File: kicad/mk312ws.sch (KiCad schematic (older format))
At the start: 14 parts, among them J1 Conn_01x06_Male, Q1 BSS138, Q2 BSS138, Q3 BSS138, Q4 BSS138, U1 mini_esp32

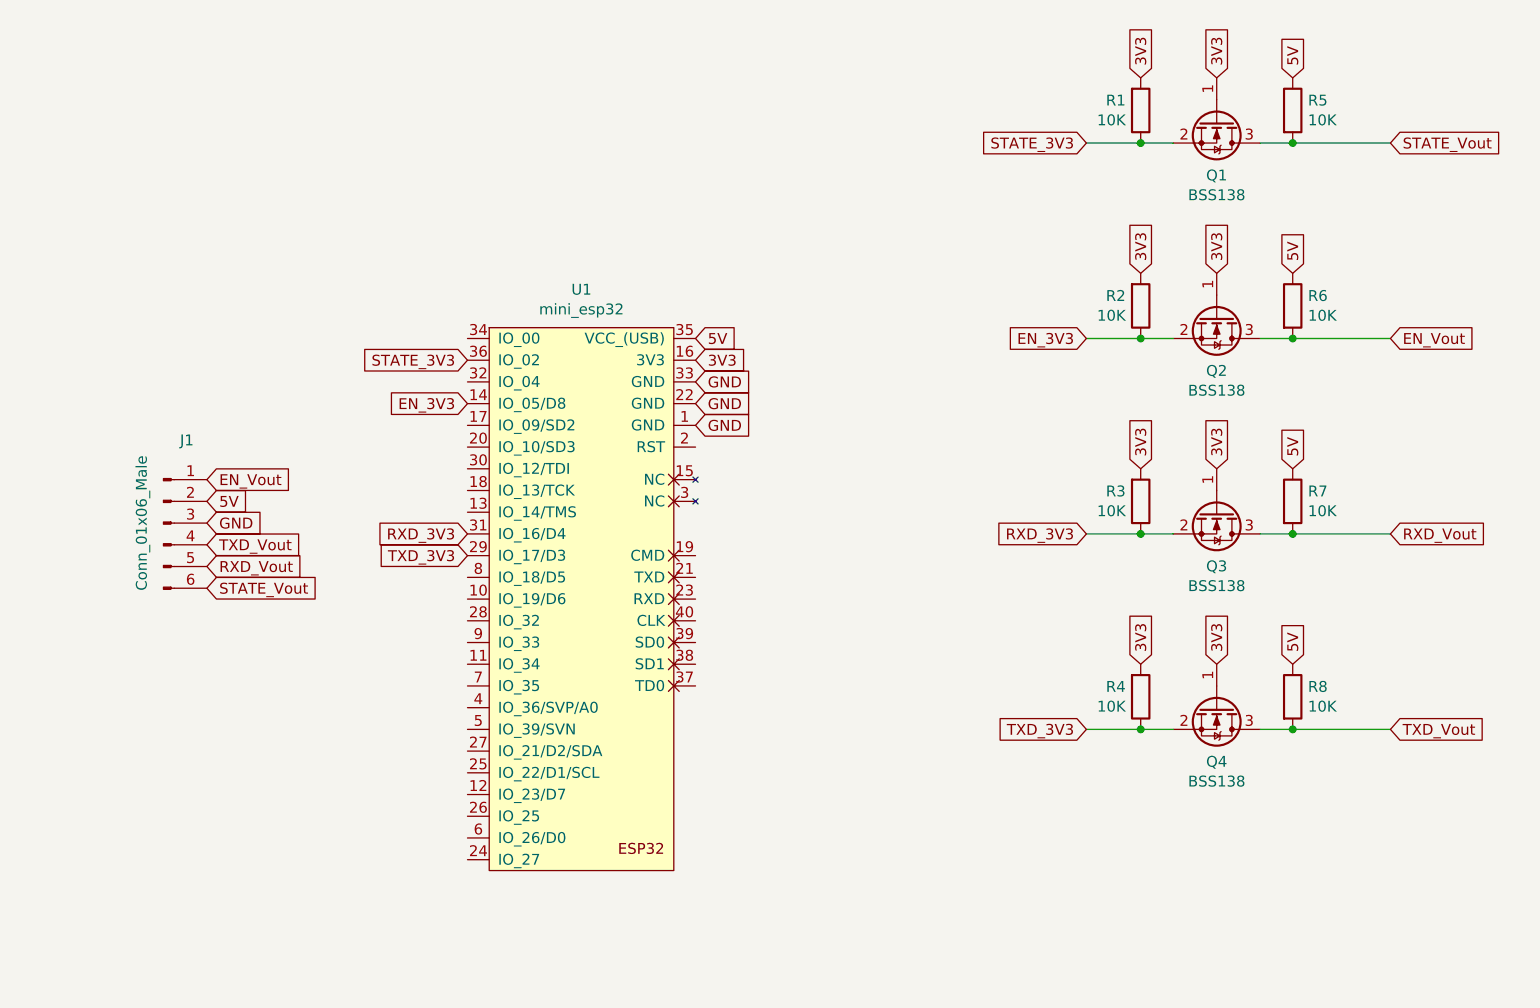
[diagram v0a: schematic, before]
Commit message: adapter v2. größere pads und jumper für serial 1 loopback
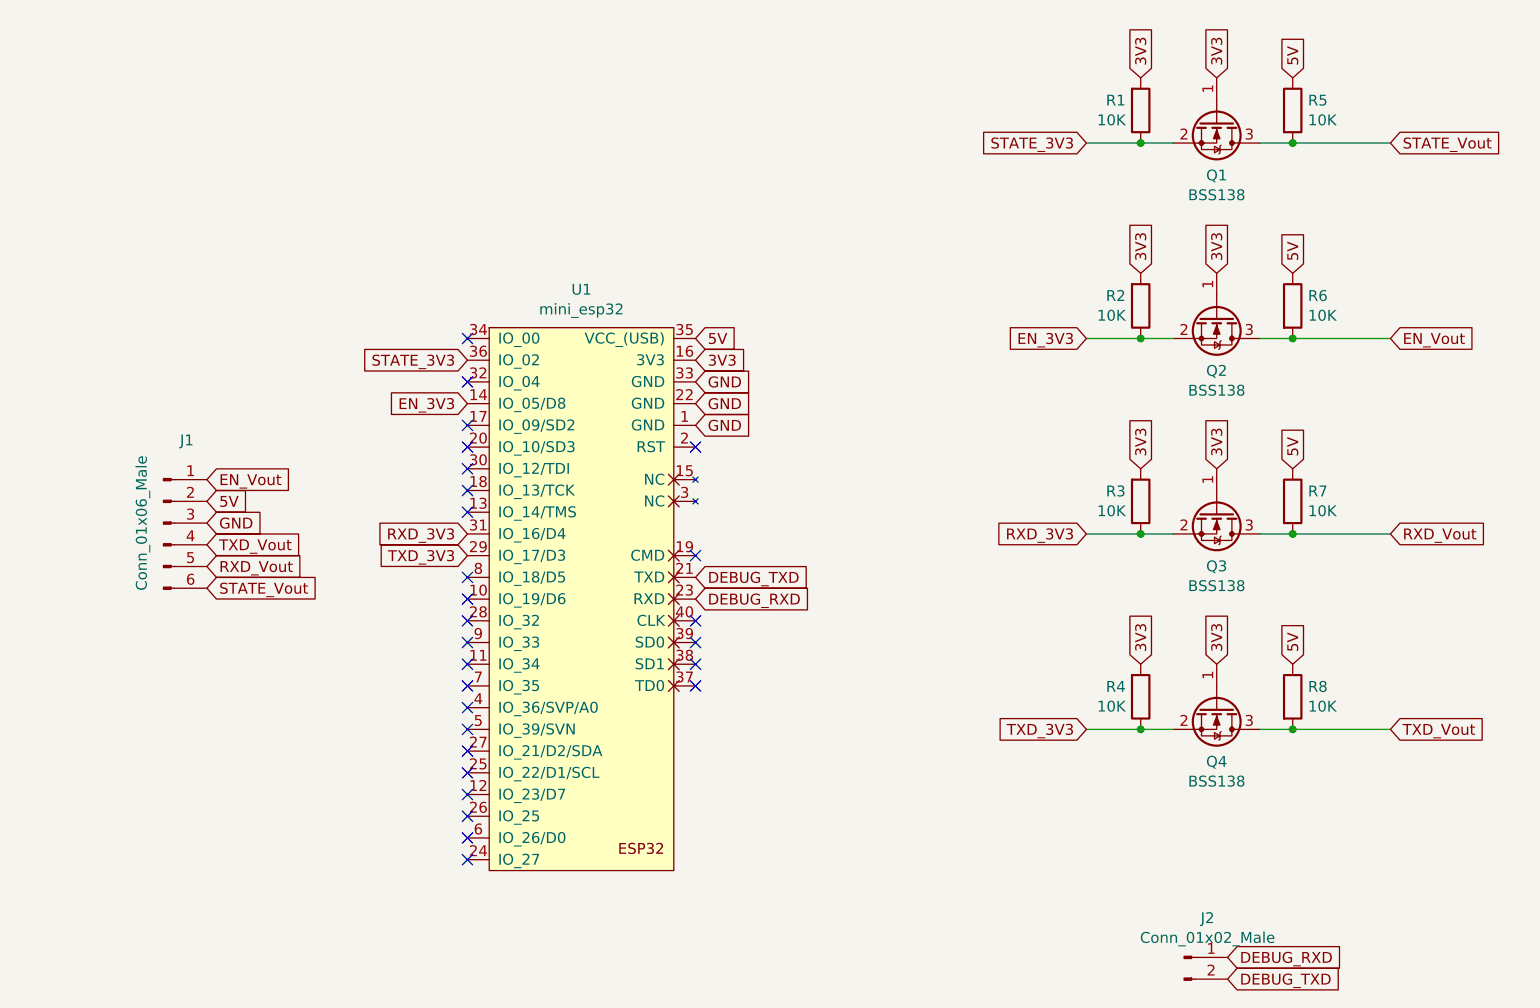
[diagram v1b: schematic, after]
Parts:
- added J2: Conn_01x02_Male, Connector_PinHeader_2.54mm:PinHeader_1x02_P2.54mm_Vertical, symbol Connector:Conn_01x02_Male
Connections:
- net DEBUG_TXD: now reaches U1.21 (TXD)
- net DEBUG_TXD: now also J2.2 (Pin_2)
- net DEBUG_RXD: now reaches U1.23 (RXD)
- net DEBUG_RXD: now also J2.1 (Pin_1)
- no-connect marks 0 -> 27
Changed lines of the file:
@@
 Text GLabel 4950 2600 0    50   Input ~ 0
 EN_3V3
+Text GLabel 6000 3400 2    50   Input ~ 0
+DEBUG_TXD
+Text GLabel 6000 3500 2    50   Input ~ 0
+DEBUG_RXD
+Text GLabel 8450 5250 2    50   Input ~ 0
+DEBUG_TXD
+Text GLabel 8450 5150 2    50   Input ~ 0
+DEBUG_RXD
+$Comp
+L Connector:Conn_01x02_Male J2
+U 1 1 60FCB3BE
+P 8250 5150
+F 0 "J2" H 8358 5331 50  0000 C CNN
+F 1 "Conn_01x02_Male" H 8358 5240 50  0000 C CNN
+F 2 "Connector_PinHeader_2.54mm:PinHeader_1x02_P2.54mm_Vertical" H 8250 5150 50  0001 C CNN
+F 3 "~" H 8250 5150 50  0001 C CNN
+	1    8250 5150
+	1    0    0    -1
+$EndComp
+NoConn ~ 6000 3300
+NoConn ~ 6000 3600
+NoConn ~ 6000 3700
+NoConn ~ 6000 3800
+NoConn ~ 6000 3900
+NoConn ~ 6000 2800
+NoConn ~ 4950 2700
+NoConn ~ 4950 2800
+NoConn ~ 4950 2900
+NoConn ~ 4950 3000
+NoConn ~ 4950 3100
+NoConn ~ 4950 3400
+NoConn ~ 4950 3500
+NoConn ~ 4950 3600
+NoConn ~ 4950 3700
+NoConn ~ 4950 3800
+NoConn ~ 4950 3900
+NoConn ~ 4950 4000
+NoConn ~ 4950 4100
+NoConn ~ 4950 4200
+NoConn ~ 4950 4300
+NoConn ~ 4950 4400
+NoConn ~ 4950 4500
+NoConn ~ 4950 4600
+NoConn ~ 4950 4700
+NoConn ~ 4950 2500
+NoConn ~ 4950 2300
 $EndSCHEMATC

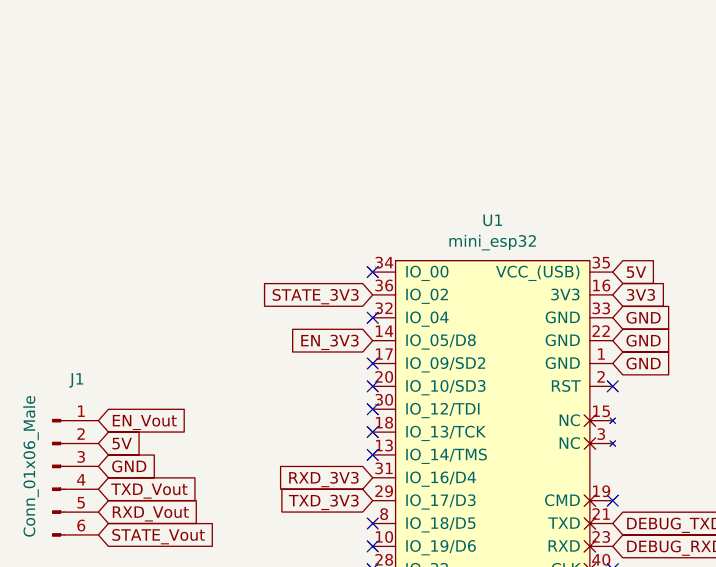
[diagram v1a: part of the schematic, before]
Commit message: kann ja keiner ahnen, dass io2 beim blitz niedrig sein muss
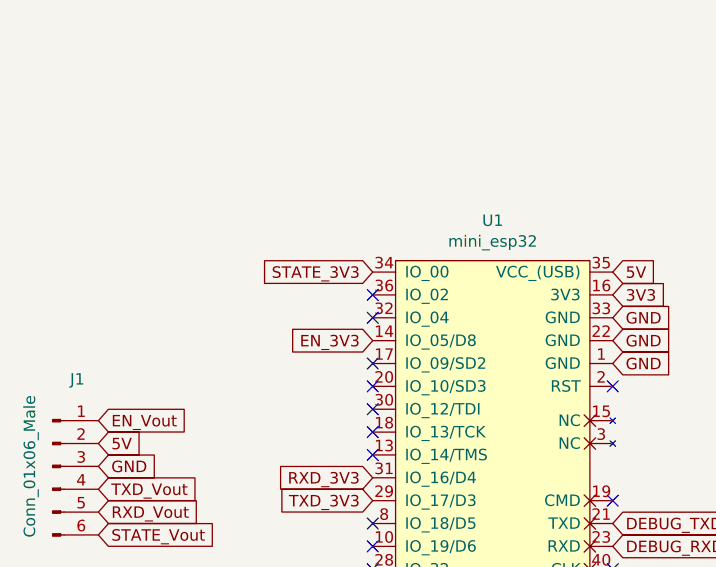
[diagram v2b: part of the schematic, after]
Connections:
- net STATE_3V3: now also U1.34 (IO_00); no longer U1.36 (IO_02)
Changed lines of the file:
@@
 Text GLabel 4950 3300 0    50   Input ~ 0
 TXD_3V3
-Text GLabel 4950 2400 0    50   Input ~ 0
+Text GLabel 4950 2300 0    50   Input ~ 0
 STATE_3V3
 Text GLabel 6000 2400 2    50   Input ~ 0
@@
 NoConn ~ 4950 4700
 NoConn ~ 4950 2500
-NoConn ~ 4950 2300
+NoConn ~ 4950 2400
 $EndSCHEMATC

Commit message: v3 mehr dinge. mehr fluten, mehr ausrichten
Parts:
- removed J2: Conn_01x02_Male, Connector_PinHeader_2.54mm:PinHeader_1x02_P2.54mm_Vertical, symbol Connector:Conn_01x02_Male
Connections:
- net DEBUG_RXD: no longer names the net of U1.23 (RXD)
- net DEBUG_TXD: no longer names the net of U1.21 (TXD)
- no-connect marks 27 -> 30
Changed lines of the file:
@@
 Text GLabel 4950 2600 0    50   Input ~ 0
 EN_3V3
-Text GLabel 6000 3400 2    50   Input ~ 0
-DEBUG_TXD
-Text GLabel 6000 3500 2    50   Input ~ 0
-DEBUG_RXD
-Text GLabel 8450 5250 2    50   Input ~ 0
-DEBUG_TXD
-Text GLabel 8450 5150 2    50   Input ~ 0
-DEBUG_RXD
-$Comp
-L Connector:Conn_01x02_Male J2
-U 1 1 60FCB3BE
-P 8250 5150
-F 0 "J2" H 8358 5331 50  0000 C CNN
-F 1 "Conn_01x02_Male" H 8358 5240 50  0000 C CNN
-F 2 "Connector_PinHeader_2.54mm:PinHeader_1x02_P2.54mm_Vertical" H 8250 5150 50  0001 C CNN
-F 3 "~" H 8250 5150 50  0001 C CNN
-	1    8250 5150
-	1    0    0    -1
-$EndComp
 NoConn ~ 6000 3300
 NoConn ~ 6000 3600
@@
 NoConn ~ 4950 2500
 NoConn ~ 4950 2400
+NoConn ~ 6000 3400
+NoConn ~ 6000 3500
+NoConn ~ 2900 1250
 $EndSCHEMATC
